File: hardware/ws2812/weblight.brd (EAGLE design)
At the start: 31.8 x 12 mm, 16 parts, among them U1 ATtiny85-20SU

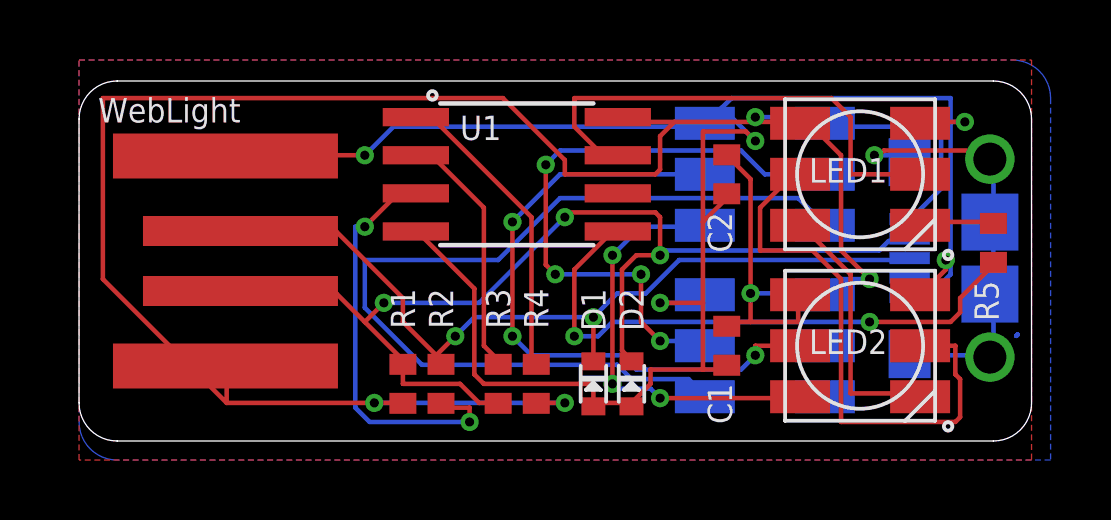
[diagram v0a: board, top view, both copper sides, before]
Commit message: Separate LED type and adopt new board versioning scheme
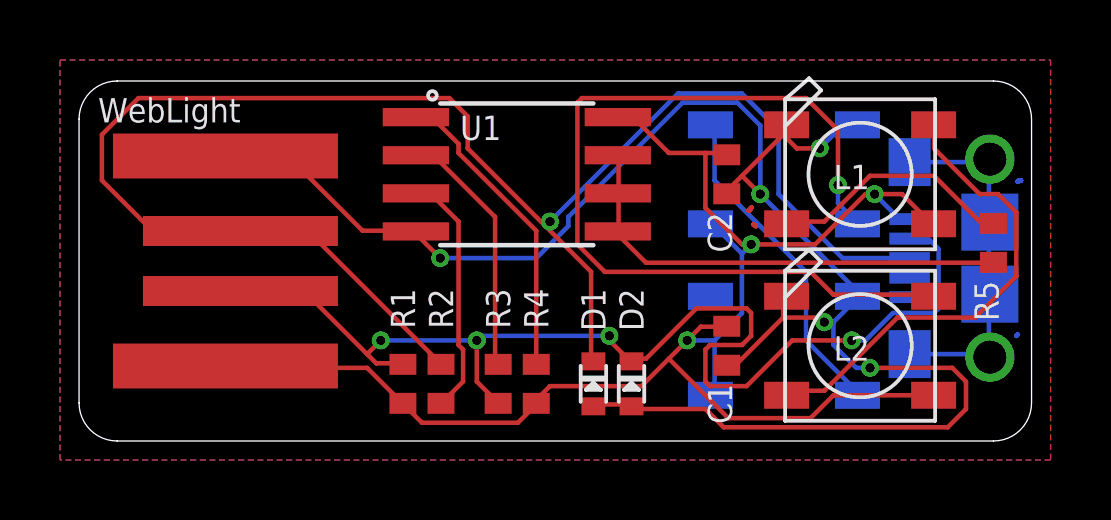
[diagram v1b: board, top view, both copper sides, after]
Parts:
- removed LED1, LED2, LED3, LED4: APA102, weblight:APA102
- added L1, L2, L3, L4: WS2812B, weblight:WS2812B
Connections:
- removed net CLK_1: LED1.CI, U1.7
- removed net CLK_2: LED1.CO, LED2.CI
- removed net CLK_3: LED2.CO, LED3.CI
- removed net CLK_4: LED3.CO, LED4.CI
- net DIN_1: now also L1.4-DIN; no longer LED1.DI
- net DIN_2: now also L1.2-DOUT, L2.4-DIN; no longer LED1.DO, LED2.DI
- net DIN_3: now also L2.2-DOUT, L3.4-DIN; no longer LED2.DO, LED3.DI
- net DIN_4: now also L3.2-DOUT, L4.4-DIN; no longer LED3.DO, LED4.DI
- net DIN_RAW: now also U1.6, U1.7
- net GND: now also L1.3-GND, L2.3-GND, L3.3-GND, L4.3-GND; no longer LED1.GND, LED2.GND, LED3.GND, LED4.GND
- net VCC: now also L1.1-VDD, L2.1-VDD, L3.1-VDD, L4.1-VDD; no longer LED1.VCC, LED2.VCC, LED3.VCC, LED4.VCC
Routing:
- net VCC: track 84.2 -> 53.5 mm, vias 5 -> 3
- net USB_D_PLUS_RAW: track 28.0 -> 55.7 mm, vias 2 -> 1
- net CLK_3: track 21.4 -> 0.00 mm, vias 3 -> 0
- net CLK_4: track 20.5 -> 0.00 mm, vias 4 -> 0
- net DIN_4: track 30.7 -> 11.1 mm
- net CLK_2: track 18.7 -> 0.00 mm
- net CLK_1: track 16.5 -> 0.00 mm
- net DIN_3: track 14.2 -> 29.9 mm, vias 3 -> 1
- net DIN_2: track 8.69 -> 15.9 mm
- net USB_D_PLUS: track 14.1 -> 8.24 mm, vias 2 -> 0
- net DIN_1: track 2.56 -> 8.27 mm
- net GND: track 68.8 -> 64.0 mm
- net DIN_RAW: track 19.5 -> 15.6 mm, vias 2 -> 0
- net N$3: track 0.00 -> 3.49 mm
- net SLD: track 15.2 -> 12.2 mm, vias 1 -> 0
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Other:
- board text added: "w-mf1"
- board text removed: "Version mf3"
